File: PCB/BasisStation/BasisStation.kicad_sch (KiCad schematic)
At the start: 20 parts, among them SW1 SW_SPST, SW4 RESET_BUTTON, U2 ESP32-S3-WROOM-2, X4 JTAG

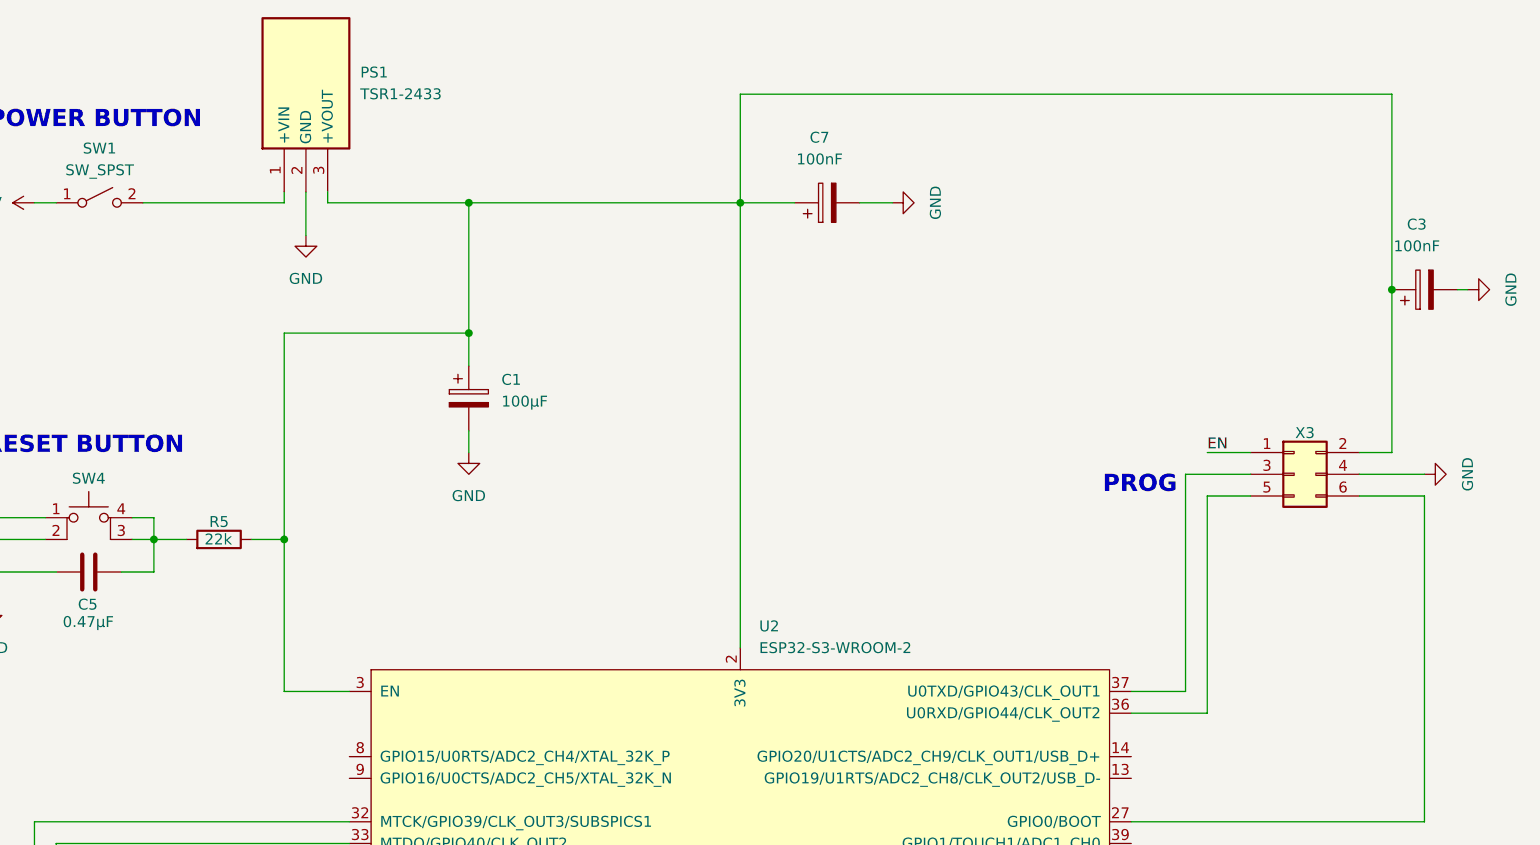
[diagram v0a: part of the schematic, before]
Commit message: Anpassung von Bauelementen
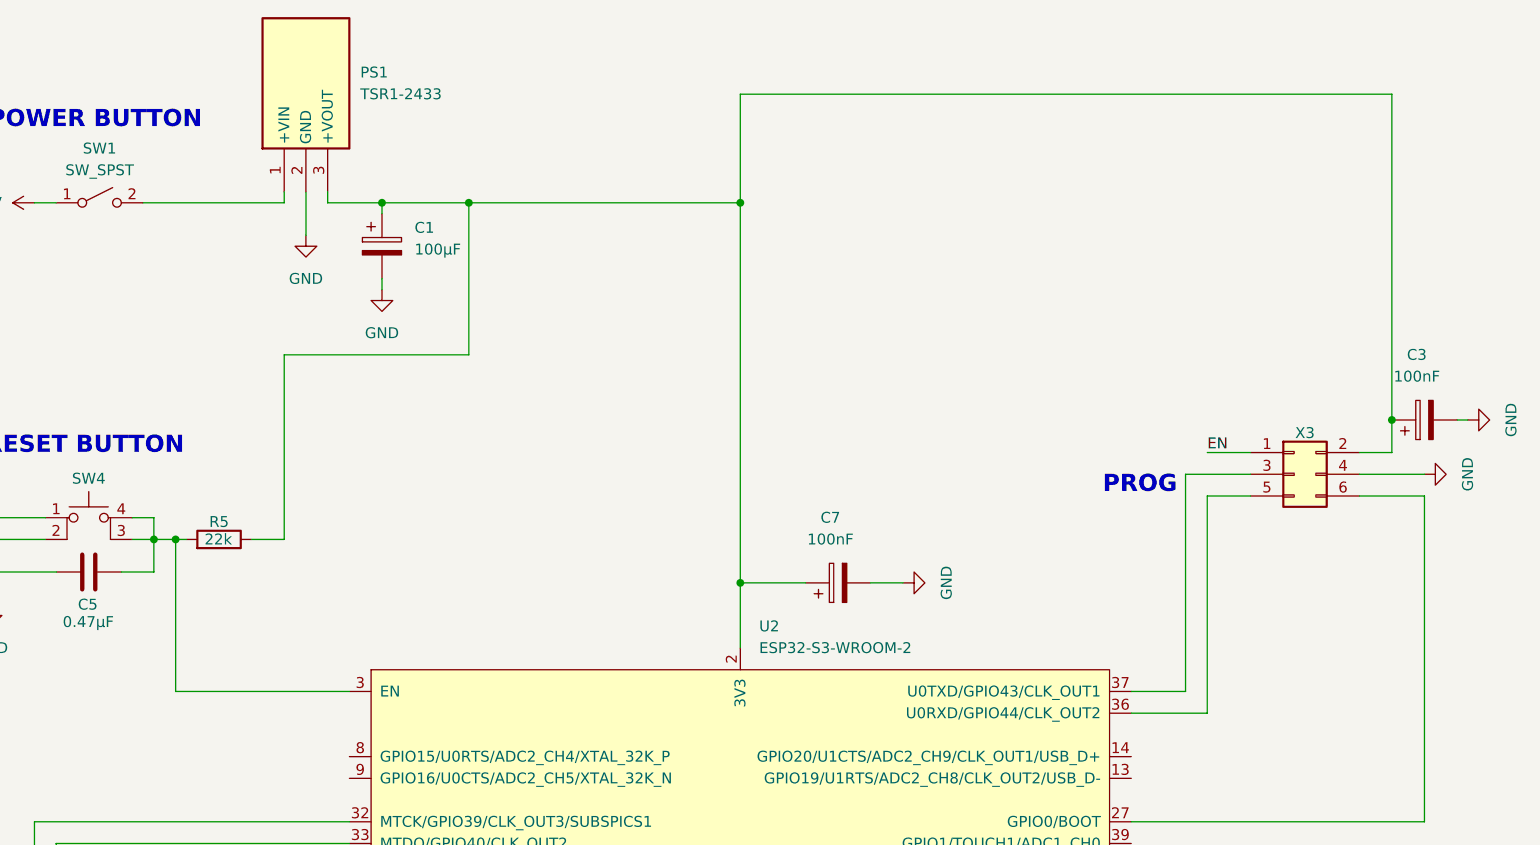
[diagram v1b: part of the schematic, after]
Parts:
- R5: footprint Resistor_THT:R_Axial_DIN0922_L20.0mm_D9.0mm_P25.40mm_Horizontal -> Resistor_THT:R_Axial_DIN0207_L6.3mm_D2.5mm_P7.62mm_Horizontal
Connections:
- net at C1.1, C3.1, C7.1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: no longer U2.3 (EN)
- net at C5.2, R5.2, SW4.3 (K)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: now also U2.3 (EN)
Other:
- moved on the sheet: C1, C3, C7

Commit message: PCB überarbeitet
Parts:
- SW1: footprint CUSTOM_Footprint:WUE_SW_471001264143_2_00-3_00_ -> (none)
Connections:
- net GND: no longer D5.1 (K), D6.1 (K), D7.1 (K), D8.1 (K)
- net at C1.1, C3.1, C7.1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: now also D5.1 (K), D6.1 (K), D7.1 (K), D8.1 (K)
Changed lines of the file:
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@@
+	)
+	(junction
+		(at 181.61 27.94)
+		(diameter 0)
+		(color 0 0 0 0)
 	)
 	(junction
@@
 	(wire
 		(pts
+			(xy 195.58 146.05) (xy 195.58 27.94)
+		)
+		(stroke
+			(width 0)
+			(type default)
+		)
+	)
+	(wire
+		(pts
 			(xy 38.1 274.32) (xy 38.1 276.86)
 		)
@@
 	(wire
 		(pts
+			(xy 195.58 27.94) (xy 181.61 27.94)
+		)
+		(stroke
+			(width 0)
+			(type default)
+		)
+	)
+	(wire
+		(pts
 			(xy 162.56 129.54) (xy 162.56 125.73)
 		)
@@
 	(wire
 		(pts
-			(xy 189.23 66.04) (xy 190.5 66.04)
+			(xy 189.23 66.04) (xy 187.96 66.04)
 		)
 		(stroke
@@
 		(pts
 			(xy 157.48 142.24) (xy 166.37 142.24)
+		)
+		(stroke
+			(width 0)
+			(type default)
+		)
+	)
+	(wire
+		(pts
+			(xy 185.42 146.05) (xy 195.58 146.05)
 		)
 		(stroke
@@
 	(symbol
 		(lib_id "power:GND")
-		(at 190.5 66.04 90)
+		(at 187.96 66.04 90)
 		(unit 1)
 		(exclude_from_sim no)
@@
 		(fields_autoplaced yes)
 		(property "Reference" "#PWR01"
-			(at 196.85 66.04 0)
+			(at 194.31 66.04 0)
 			(effects
 				(font
@@
 		)
 		(property "Value" "GND"
-			(at 195.58 66.04 0)
+			(at 193.04 66.04 0)
 			(effects
 				(font
@@
 		)
 		(property "Footprint" ""
-			(at 190.5 66.04 0)
+			(at 187.96 66.04 0)
 			(effects
 				(font
@@
 		)
 		(property "Datasheet" ""
-			(at 190.5 66.04 0)
+			(at 187.96 66.04 0)
 			(effects
 				(font
@@
 		)
 		(property "Description" "Power symbol creates a global label with name \"GND\" , ground"
-			(at 190.5 66.04 0)
+			(at 187.96 66.04 0)
 			(effects
 				(font
@@
 			)
 		)
-		(property "Footprint" "CUSTOM_Footprint:WUE_SW_471001264143_2_00-3_00_"
+		(property "Footprint" ""
 			(at 30.48 40.64 0)
 			(effects
@@
 					(unit 1)
 				)
-			)
-		)
-	)
-	(symbol
-		(lib_id "power:GND")
-		(at 185.42 146.05 0)
-		(unit 1)
-		(exclude_from_sim no)
-		(in_bom yes)
-		(on_board yes)
-		(dnp no)
-		(property "Reference" "#PWR03"
-			(at 185.42 152.4 0)
-			(effects
-				(font
-					(size 1.27 1.27)
-				)
-				(hide yes)
-			)
-		)
-		(property "Value" "GND"
-			(at 185.42 150.368 0)
-			(effects
-				(font
-					(size 1.27 1.27)
-				)
-			)
-		)
-		(property "Footprint" ""
-			(at 185.42 146.05 0)
-			(effects
-				(font
-					(size 1.27 1.27)
-				)
-				(hide yes)
-			)
-		)
-		(property "Datasheet" ""
-			(at 185.42 146.05 0)
-			(effects
-				(font
-					(size 1.27 1.27)
-				)
-				(hide yes)
-			)
-		)
-		(property "Description" "Power symbol creates a global label with name \"GND\" , ground"
-			(at 185.42 146.05 0)
-			(effects
-				(font
-					(size 1.27 1.27)
-				)
-				(hide yes)
-			)
-		)
-		(pin "1"
-		)
-		(instances
-			(project "BasisStation"
-				(path "/cc03a18a-a128-4e00-a998-441923eeacd1"
-					(reference "#PWR03")
-					(unit 1)
-				)

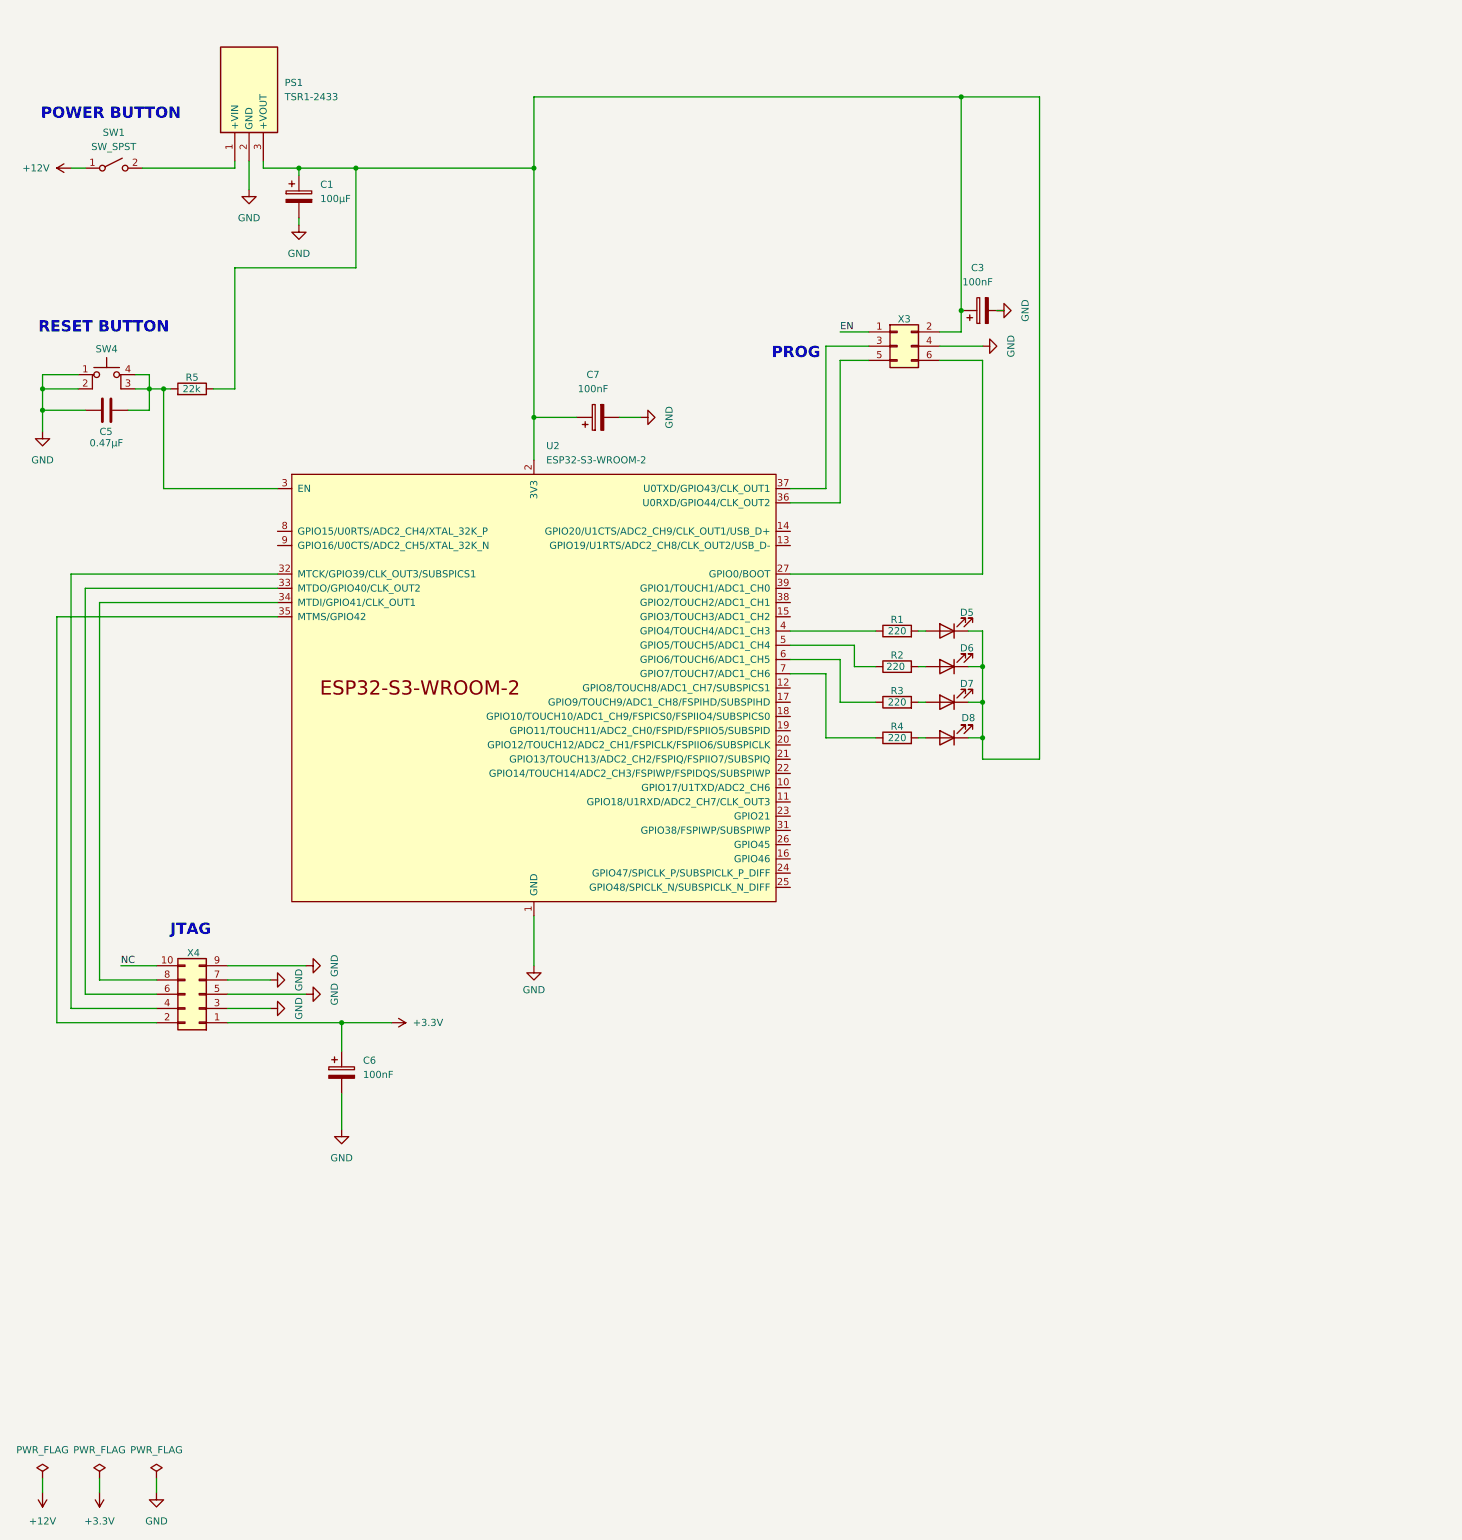
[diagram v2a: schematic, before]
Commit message: Alte Schaltpläne gelöscht und neue erstellt
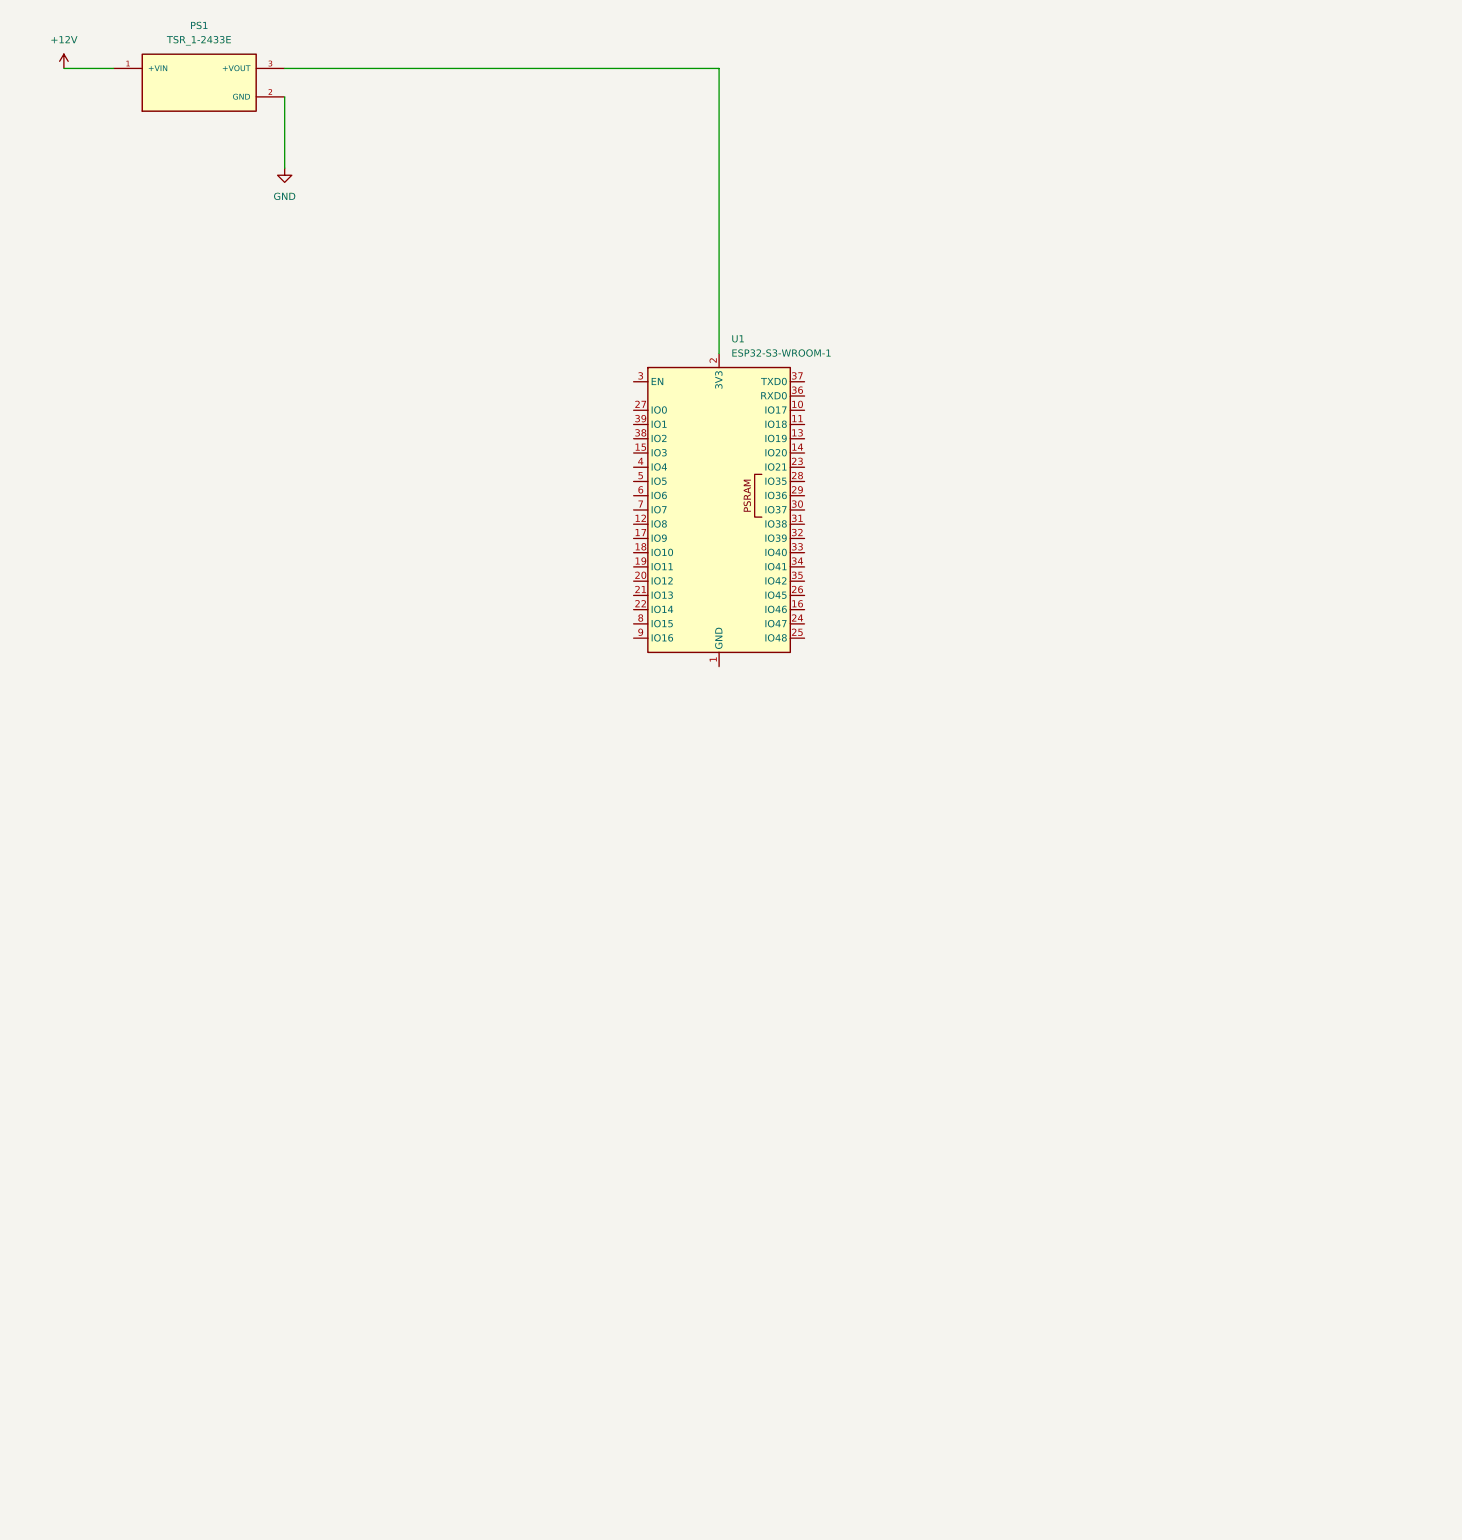
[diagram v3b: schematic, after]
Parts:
- removed C1: 100µF, Capacitor_THT:CP_Radial_D6.3mm_P2.50mm, symbol Device:C_Polarized
- removed C3, C6, C7: 100nF, Capacitor_THT:CP_Radial_D6.3mm_P2.50mm, symbol Device:C_Polarized
- removed C5: 0.47µF, CUSTOM_Footprint:CAPAE530X565N, symbol Device:C
- removed D5, D6, D7, D8: LED, CUSTOM_Footprint:LED-RED-3MM-ROUND, symbol Device:LED
- removed PS1: TSR1-2433, TSR1-2433:TSR12433, symbol TSR1-2433:TSR1-2433
- removed R1, R2, R3, R4: 220, Resistor_THT:R_Axial_DIN0309_L9.0mm_D3.2mm_P12.70mm_Horizontal, symbol Device:R
- removed R5: 22k, Resistor_THT:R_Axial_DIN0207_L6.3mm_D2.5mm_P7.62mm_Horizontal, symbol Device:R
- removed SW1: SW_SPST, symbol Switch:SW_SPST
- removed SW4: RESET_BUTTON, Button_Switch_THT:SW_PUSH_1P1T_6x3.5mm_H4.3_APEM_MJTP1243, symbol Switch:SW_MEC_5E
- removed U2: ESP32-S3-WROOM-2, PCM_Espressif:ESP32-S3-WROOM-2, symbol PCM_Espressif:ESP32-S3-WROOM-2
- removed X3: ~, Connector_PinHeader_2.54mm:PinHeader_2x03_P2.54mm_Vertical, symbol Connector_Generic:Conn_02x03_Odd_Even
- removed X4: JTAG, CUSTOM_Footprint:WUE_CONNECTOR_SHDR10W64P254_2X5_2036X885X925P, symbol Connector_Generic:Conn_02x05_Odd_Even
- added PS1: TSR_1-2433E, Footprints:CONV_TSR_1-2433E, symbol TSR_1-2433E:TSR_1-2433E
- added U1: ESP32-S3-WROOM-1, RF_Module:ESP32-S3-WROOM-1, symbol RF_Module:ESP32-S3-WROOM-1
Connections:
- net +12V: now also PS1.1 (+VIN)
- net GND: now also PS1.2 (GND)
- new net: PS1.3 (+VOUT), U1.2 (3V3)
- new net: U1.1 (GND), U1.40 (GND), U1.41 (GND)
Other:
- note removed: "JTAG"
- note removed: "POWER BUTTON"
- note removed: "PROG"
- note removed: "RESET BUTTON"
- company: Zott-IT -> (none)
- title: HomeSystem - Base Station -> (none)
